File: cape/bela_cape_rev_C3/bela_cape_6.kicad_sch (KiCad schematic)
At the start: 57 parts, among them IC4 MC33204, IC5 MC33204, IC6 ES9080Q, J12 Conn_01x03, J13 Conn_01x03, J14 Conn_01x03, J15 Conn_01x03

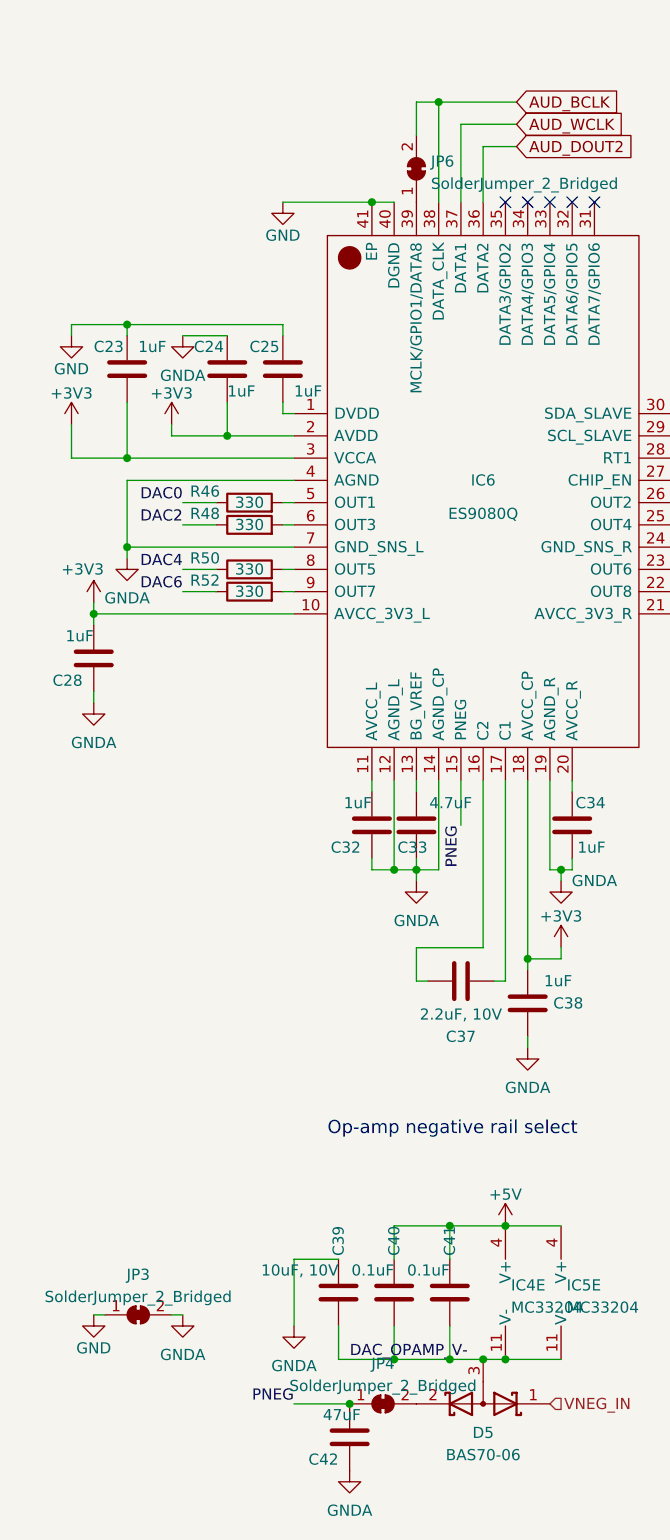
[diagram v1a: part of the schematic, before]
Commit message: removed sym-lib-table with a reference to an unused and obsolete local library
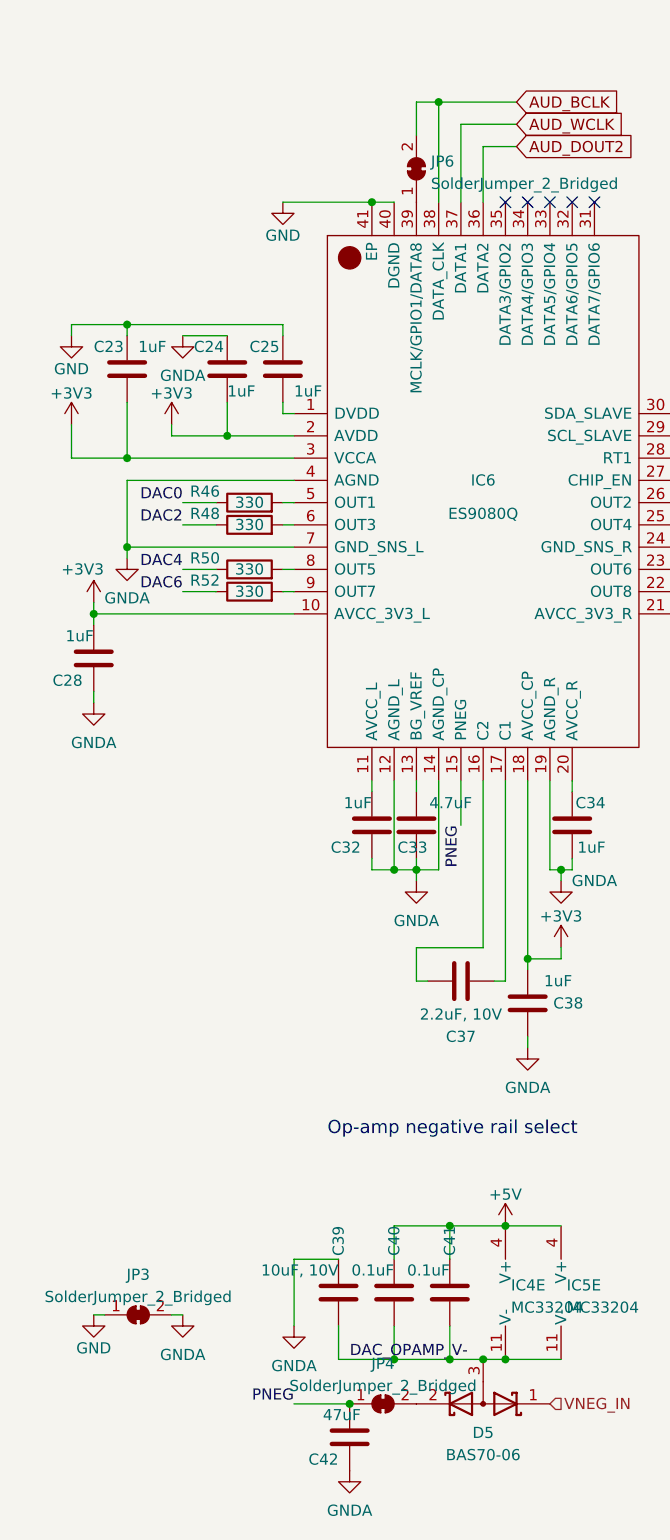
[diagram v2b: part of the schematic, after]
